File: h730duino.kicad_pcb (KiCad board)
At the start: 4 copper layers, 101.6 x 53.3 mm, 124 parts, among them J1 USB_C_Receptacle_USB2.0, J2 USB_B_Micro, J3 L834-1G1T-91, J4 105162-0001, J5 Conn_ARM_JTAG_SWD_10, J6 Conn_ARM_JTAG_SWD_10, P1 CONN_02x18, P10 CONN_01X01, P11 CONN_01X01, P13 CONN_01X01, P2 CONN_01x08, P3 CONN_01x08, P4 CONN_01x08, P5 CONN_01x10, P6 CONN_01x08, P7 CONN_01x08, P8 CONN_01X01, SW1 RESET, U1 STM32H730ZBT6, U10 S27KL0641DABHI020, U12 AP2161W, U2 IS25LP032D-JBLE-TR, U3 TPS62162DSG, U4 TPS62163DSG, U5 MAX40200AUK, U6 MAX40200AUK, U7 STM32F048G6Ux, U8 MAX40200AUK, U9 LAN8742A, Y1 32.768K, Y2 8M, Y3 25M

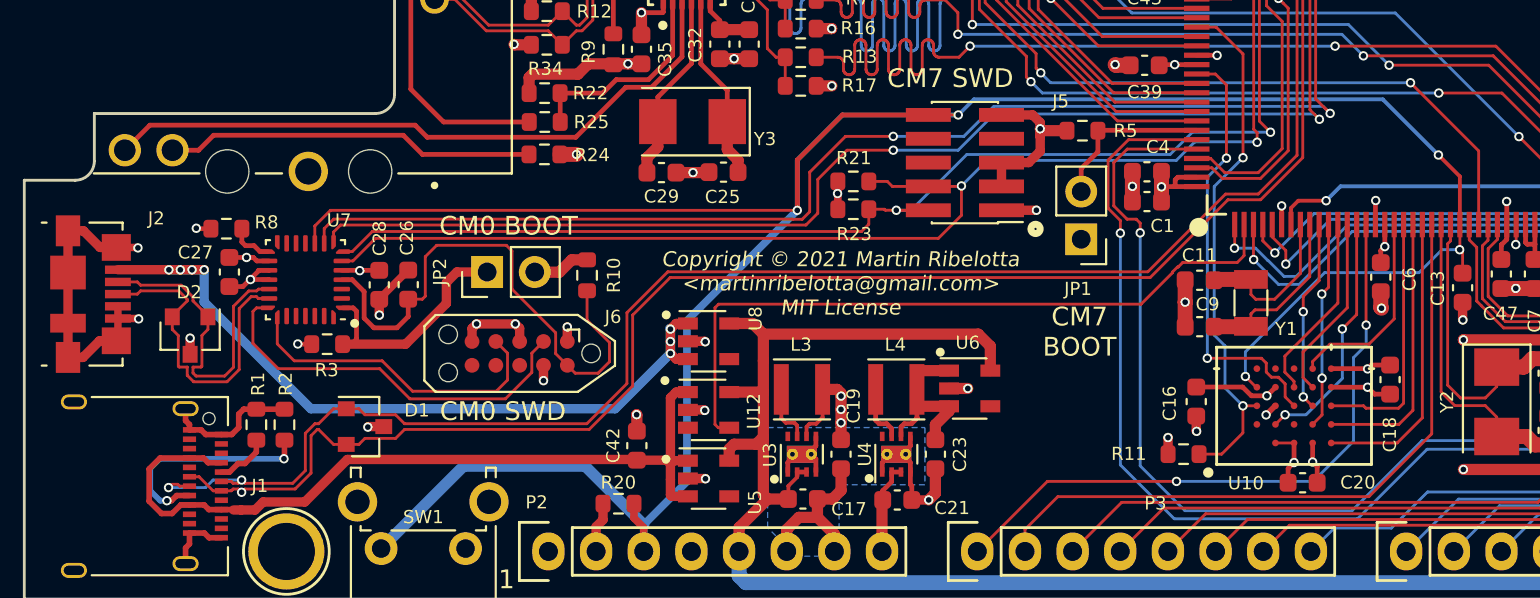
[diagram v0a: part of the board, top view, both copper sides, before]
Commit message: Fix 1V8 issue and OSPI pinout
Signed-off-by: Martin Ribelotta <martinribelotta@gmail.com>
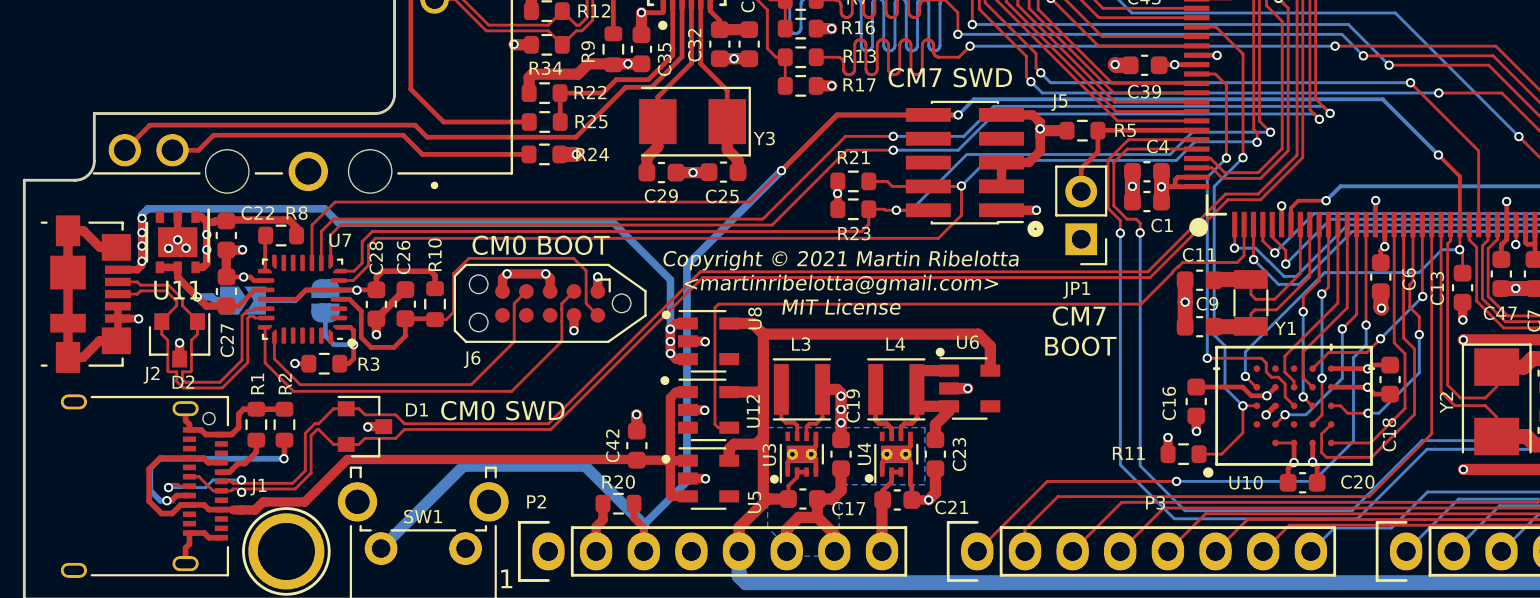
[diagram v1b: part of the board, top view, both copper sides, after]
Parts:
- added C22: 1u, Capacitor_SMD:C_0603_1608Metric, F.Cu at (114.1, 102.3)
- added JP3: Jumper_NO_Small, Jumper:SolderJumper-2_P1.3mm_Open_TrianglePad1.0x1.5mm, B.Cu at (115.0, 105.8)
- added U11: LP38691SD-1.8, Package_SON:WSON-6-1EP_3x3mm_P0.95mm, F.Cu at (111.6, 102.6)
- C27: value 100n -> 1u
- JP2: footprint Connector_PinHeader_2.54mm:PinHeader_1x02_P2.54mm_Vertical -> Jumper:SolderJumper-2_P1.3mm_Open_RoundedPad1.0x1.5mm; moved to B.Cu
- moved JP2 8.75 mm to (119.4, 105.8)
- moved R10 8.25 mm to (125.3, 105.9)
- moved J6 3.12 mm to (131.4, 105.9)
- moved R8 2.94 mm to (117.1, 102.3), turned to 180 degrees
- moved C26 1.05 mm to (123.7, 105.9)
- moved C27 1.05 mm to (114.2, 105.3)
- moved C28 1.05 mm to (122.1, 106.0)
- moved R3 1.05 mm to (119.4, 109.1)
- moved U7 1.05 mm to (118.2, 105.7)
- moved D2 0.61 mm to (111.7, 107.9)
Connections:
- C27 pad 1: +3V3 -> Net-(C27-Pad1)
- U10 pad D5: /OCTOSPIM_P1_IO3 -> /OCTOSPIM_P1_IO1
- U10 pad E1: /OCTOSPIM_P1_IO1 -> /OCTOSPIM_P1_IO3
- U10 pad E2: /OCTOSPIM_P1_IO0 -> /OCTOSPIM_P1_IO2
- U10 pad E3: /OCTOSPIM_P1_IO2 -> /OCTOSPIM_P1_IO0
- U7 pad 17: +3V3 -> Net-(C27-Pad1)
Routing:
- net +3V3: track 117.0 -> 133.0 mm
- net Net-(C27-Pad1): track 0.00 -> 8.99 mm, vias 0 -> 1
- net /Debug/~DBGR: track 29.0 -> 21.7 mm
- net /Debug/DBGB: track 13.1 -> 6.07 mm, vias 0 -> 1
- net /OCTOSPIM_P1_IO2: track 13.5 -> 18.1 mm
- net /OCTOSPIM_P1_IO1: track 15.7 -> 11.3 mm, vias 0 -> 2
- net /OCTOSPIM_P1_IO3: track 10.7 -> 14.7 mm
- net /DBG_VBUS: track 41.4 -> 44.9 mm
- net GND: track 177.6 -> 180.7 mm, vias 72 -> 75
- net /USB_OTG_HS_N: track 89.7 -> 87.5 mm
- net /USB_OTG_HS_P: track 92.5 -> 90.3 mm
- net /SWDIO: track 71.3 -> 72.5 mm
- net /SWCLK: track 74.4 -> 75.6 mm
- net /Debug/DBG_SWDIO: track 21.2 -> 22.4 mm
- net /Debug/DBG_SWCK: track 17.3 -> 18.4 mm
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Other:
- rule via_min_drill: 0.2 -> 0.3

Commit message: REally fix HyperRAM connection.
Additionally:
 - Fix PTH on ETH connector
 - Move USB-C to the left

Signed-off-by: Martin Ribelotta <martinribelotta@gmail.com>
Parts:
- LOGO1: footprint Symbol:OSHW-Logo_5.7x6mm_SilkScreen -> Symbol:OSHW-Logo_7.5x8mm_SilkScreen
- moved LOGO1 2.26 mm to (154.4, 83.9)
- moved JP3 2.16 mm to (113.1, 104.8), turned to 90 degrees
- moved C41 0.85 mm to (116.6, 79.1)
- moved C22 0.63 mm to (114.5, 102.8)
- moved C27 0.50 mm to (113.7, 105.3), turned to 0 degrees
- moved J1 0.25 mm to (108.6, 115.6)
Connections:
- SW1 pad 1: GND -> /~RST
- SW1 pad 2: /~RST -> GND
- U10 pad D5: /OCTOSPIM_P1_IO1 -> /OCTOSPIM_P1_IO0
- U10 pad E3: /OCTOSPIM_P1_IO0 -> /OCTOSPIM_P1_IO1
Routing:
- net /~RST: track 142.6 -> 135.7 mm
- net +3V3: track 133.0 -> 128.8 mm, vias 36 -> 37
- net /OCTOSPIM_P1_IO1: track 11.3 -> 14.7 mm
- net /OCTOSPIM_P1_IO0: track 13.9 -> 11.6 mm
- net /SWDIO: track 72.5 -> 71.8 mm
- net Net-(J1-PadB5): track 12.0 -> 11.3 mm
- net /SWCLK: track 75.6 -> 75.0 mm
- net /USART1_RX: track 73.5 -> 72.9 mm
- net /USART1_TX: track 74.6 -> 74.1 mm
- net /DBG_VBUS: track 44.9 -> 44.4 mm
- net Net-(J4-Pad2): track 15.0 -> 14.5 mm
- net Net-(C27-Pad1): track 8.99 -> 9.50 mm
- net GND: track 180.7 -> 180.3 mm, vias 75 -> 74
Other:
- board text removed: "CM0 BOOT"

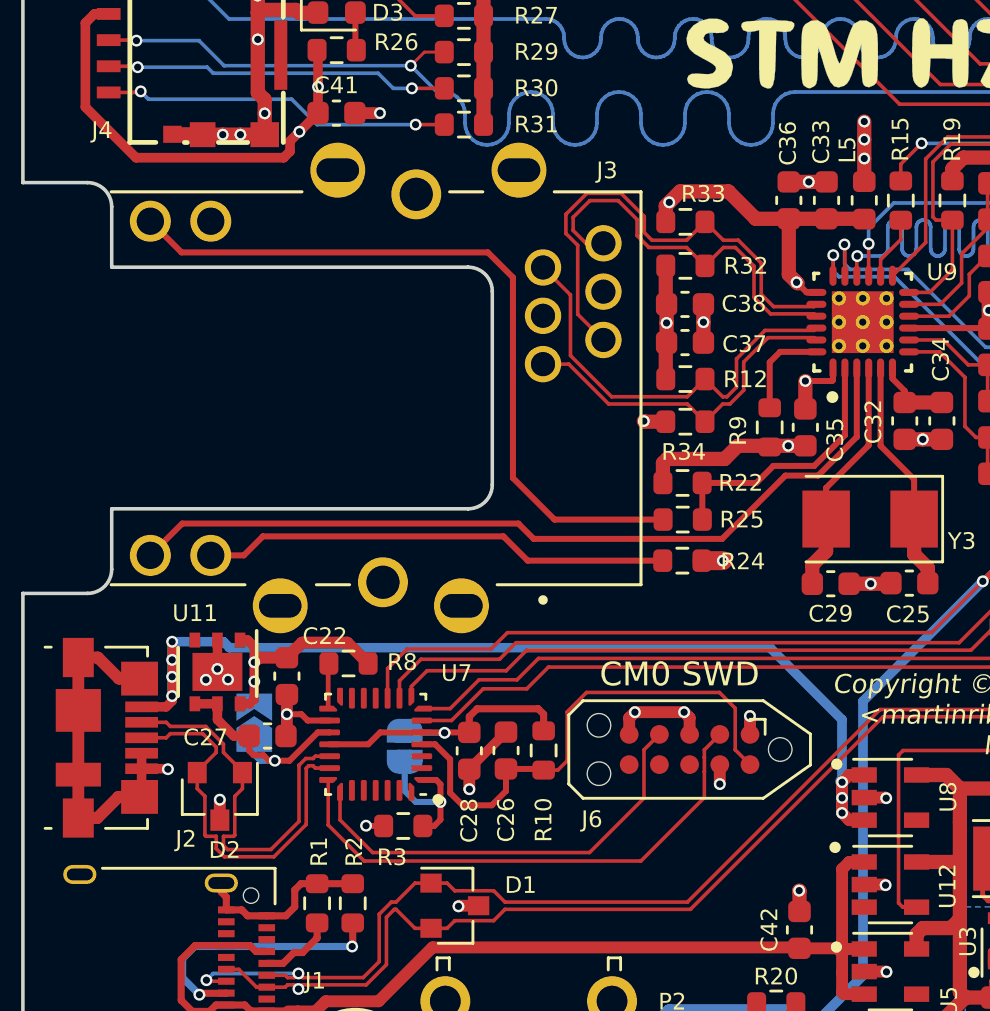
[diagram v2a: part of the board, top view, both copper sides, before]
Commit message: Change 1V8 regulator for a more cheap and small part
Signed-off-by: Martin Ribelotta <martinribelotta@gmail.com>
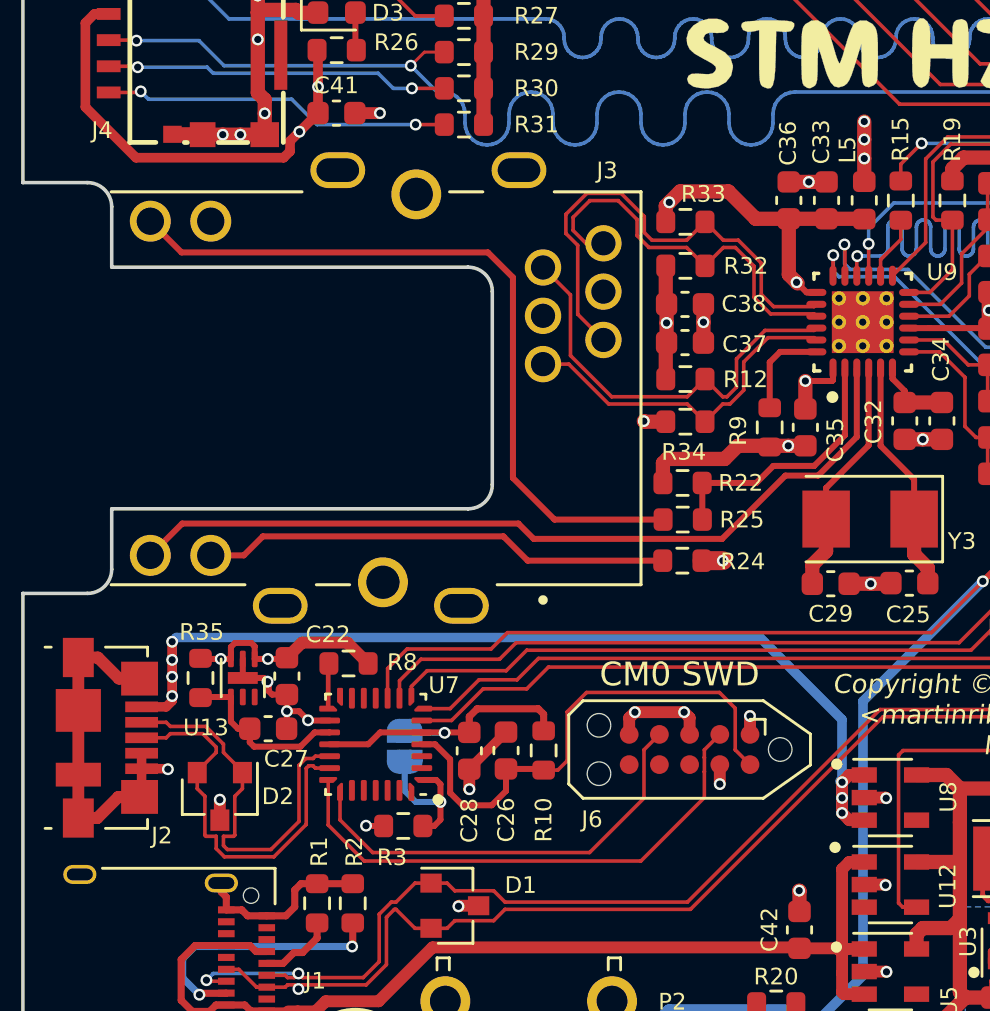
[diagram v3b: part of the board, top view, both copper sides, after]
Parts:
- removed JP3: Jumper_NO_Small, Jumper:SolderJumper-2_P1.3mm_Open_TrianglePad1.0x1.5mm
- removed U11: LP38691SD-1.8, Package_SON:WSON-6-1EP_3x3mm_P0.95mm
- added R35: 0R, Resistor_SMD:R_0603_1608Metric, F.Cu at (110.8, 102.9)
- added U13: MIC5353-1.8YMT, Package_DFN_QFN:MLF-6-1EP_1.6x1.6mm_P0.5mm_EP0.5x1.26mm, F.Cu at (112.6, 102.9)
- moved C27 0.31 mm to (113.7, 105.0)
- turned C22 to 90 degrees
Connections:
- C22 pad 1: +3V3 -> GND
- C22 pad 2: GND -> +3V3
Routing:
- net Net-(C27-Pad1): track 9.50 -> 7.49 mm, vias 1 -> 0
- net +3V3: track 128.8 -> 127.6 mm
- net GND: track 180.3 -> 181.2 mm, vias 74 -> 73
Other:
- board text added: "Short for normal DAP operation"

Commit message: Some changes
Signed-off-by: Martin Ribelotta <martinribelotta@gmail.com>
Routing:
- net /OCTOSPIM_P1_IO2: track 18.0 -> 13.9 mm, vias 0 -> 2
- net /OCTOSPIM_P1_IO3: track 15.1 -> 13.9 mm, vias 0 -> 2
- net GND: track 181.2 -> 182.1 mm
- net +3V3: track 127.6 -> 128.5 mm
- net /OCTOSPIM_P1_IO0: track 11.6 -> 12.1 mm, vias 2 -> 0
- net /OCTOSPIM_P1_IO1: track 14.7 -> 14.3 mm, vias 2 -> 0

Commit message: Add QR of project URL
Signed-off-by: Martin Ribelotta <martinribelotta@gmail.com>
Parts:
- removed C22, C27: 1u, Capacitor_SMD:C_0603_1608Metric
- removed C26, C28: 100n, Capacitor_SMD:C_0603_1608Metric
- removed D2: SP0502BAHT, Package_TO_SOT_SMD:SOT-23
- removed J5: Conn_ARM_JTAG_SWD_10, Connector_PinHeader_1.27mm:PinHeader_2x05_P1.27mm_Vertical_SMD
- removed J6: Conn_ARM_JTAG_SWD_10, Connector:Tag-Connect_TC2050-IDC-NL_2x05_P1.27mm_Vertical
- removed JP2: Jumper_NO_Small, Jumper:SolderJumper-2_P1.3mm_Open_RoundedPad1.0x1.5mm
- removed R10, R21, R23, R3, R8: 10K, Resistor_SMD:R_0603_1608Metric
- removed R35: 0R, Resistor_SMD:R_0603_1608Metric
- removed U13: MIC5353-1.8YMT, Package_DFN_QFN:MLF-6-1EP_1.6x1.6mm_P0.5mm_EP0.5x1.26mm
- removed U7: STM32F048G6Ux, Package_DFN_QFN:QFN-28_4x4mm_P0.5mm
- removed U8: MAX40200AUK, Package_TO_SOT_SMD:SOT-23-5
- added QR1: https://github.com/martinribelotta/h730duino, footprints:url_qr, B.Cu at (138.2, 102.9)
- J2: value USB_B_Micro -> Conn_02x03_Odd_Even; footprint Connector_USB:USB_Micro-B_Molex_47346-0001 -> Connector_PinHeader_2.54mm:PinHeader_2x03_P2.54mm_Horizontal
- moved C16 11.7 mm to (177.5, 112.2)
- moved J2 9.86 mm to (116.5, 107.8), turned to 180 degrees
- moved JP1 7.06 mm to (153.6, 99.0), turned to 90 degrees
- moved C18 7.02 mm to (169.2, 109.4), turned to 270 degrees
- moved R5 6.67 mm to (155.3, 101.6)
- moved U6 5.28 mm to (149.9, 106.9), turned to 180 degrees
- moved R11 4.75 mm to (166.8, 109.5), turned to 270 degrees
- moved C20 3.84 mm to (169.2, 112.4), turned to 90 degrees
- moved U10 2.37 mm to (173.4, 112.0), turned to 180 degrees
- moved G1 1.81 mm to (145.8, 77.2)
- moved D1 1.43 mm to (121.9, 111.1)
- moved Y1 1.38 mm to (170.0, 105.3)
- moved C11 1.38 mm to (167.3, 104.1)
- moved C9 1.38 mm to (167.3, 106.6)
- moved D4 1.22 mm to (202.5, 101.2)
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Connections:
- J1 pad A8: (no net) -> Net-(J1-PadA8)
- J1 pad B8: (no net) -> Net-(J1-PadB8)
- J2 pad 1: /DBG_VBUS -> /~RST
- J2 pad 2: /Debug/USBD_D- -> GND
- J2 pad 3: /Debug/USBD_D+ -> /USART1_RX
- J2 pad 4: GND -> /SWDIO
- J2 pad 5: GND -> /USART1_TX
- J2 pad 6: GND -> /SWCLK
- P10 pad 1: (no net) -> Net-(P10-Pad1)
- P11 pad 1: (no net) -> Net-(P11-Pad1)
- P13 pad 1: (no net) -> Net-(P13-Pad1)
- P2 pad 1: (no net) -> Net-(P2-Pad1)
- P8 pad 1: (no net) -> Net-(P8-Pad1)
- U10 pad A2: (no net) -> Net-(U10-PadA2)
- U10 pad A5: (no net) -> Net-(U10-PadA5)
- U10 pad B5: (no net) -> Net-(U10-PadB5)
- U10 pad C2: (no net) -> Net-(U10-PadC2)
- U10 pad C4: /OCTOSPIM_P2_IO2 -> /OCTOSPIM_P1_IO2
- U10 pad C5: (no net) -> Net-(U10-PadC5)
- U10 pad D2: /OCTOSPIM_P2_IO1 -> /OCTOSPIM_P1_IO1
- U10 pad D3: /OCTOSPIM_P2_IO0 -> /OCTOSPIM_P1_IO0
- U10 pad D4: /OCTOSPIM_P2_IO3 -> /OCTOSPIM_P1_IO3
- U10 pad D5: /OCTOSPIM_P1_IO0 -> /OCTOSPIM_P2_IO0
- U10 pad E1: /OCTOSPIM_P1_IO3 -> /OCTOSPIM_P2_IO3
- U10 pad E2: /OCTOSPIM_P1_IO2 -> /OCTOSPIM_P2_IO2
- U10 pad E3: /OCTOSPIM_P1_IO1 -> /OCTOSPIM_P2_IO1
- U12 pad 3: (no net) -> Net-(U12-Pad3)
- U3 pad 8: (no net) -> Net-(U3-Pad8)
- U4 pad 8: (no net) -> Net-(U4-Pad8)
- U5 pad 4: (no net) -> Net-(U5-Pad4)
- U6 pad 4: (no net) -> Net-(U6-Pad4)
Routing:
- net /~RST: track 135.7 -> 91.1 mm, vias 5 -> 2
- net /DBG_VBUS: track 44.5 -> 0.00 mm, vias 7 -> 0
- net GND: track 182.1 -> 151.0 mm, vias 73 -> 64
- net +3V3: track 128.5 -> 103.9 mm, vias 37 -> 30
- net /Debug/DBG_SWDIO: track 22.4 -> 0.00 mm
- net /Debug/~DBGR: track 21.7 -> 0.00 mm
- net /Debug/DBG_SWCK: track 18.4 -> 0.00 mm
- net /Debug/USBD_D+: track 16.5 -> 0.00 mm
- net /Debug/USBD_D-: track 16.5 -> 0.00 mm
- net +5V: track 148.6 -> 137.8 mm
- net Net-(C27-Pad1): track 7.49 -> 0.00 mm
- net /Debug/DBGB: track 6.07 -> 0.00 mm, vias 1 -> 0
- net /BOOT0: track 8.89 -> 14.0 mm
- net /SWDIO: track 71.8 -> 76.8 mm, vias 2 -> 1
- net /OCTOSPIM_P2_NCS: track 28.1 -> 32.9 mm
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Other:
- rule trace_min: 0.127 -> 0.1524
- board text added: "BOOT"
- board text added: "MIT License Copyright © 2021 by Martin Ribelotta martinribelotta@gmail.com"
- board text added: "SWCLK SWDIO GND"
- board text added: "U1-TX U1-RX ~RST"
- board text removed: "CM0 SWD"
- board text removed: "CM7 BOOT"
- board text removed: "CM7 SWD"
- board text removed: "Copyright © 2021 Martin Ribelotta <martinribelotta@gmail.com> MIT License"
- board text removed: "Short for normal DAP operation"
